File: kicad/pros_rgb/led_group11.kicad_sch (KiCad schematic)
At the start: 7 parts

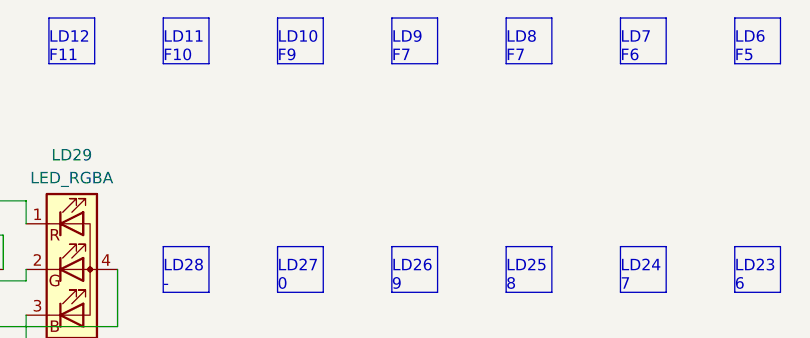
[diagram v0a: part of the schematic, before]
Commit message: kicad/pros_rgb: fix typos
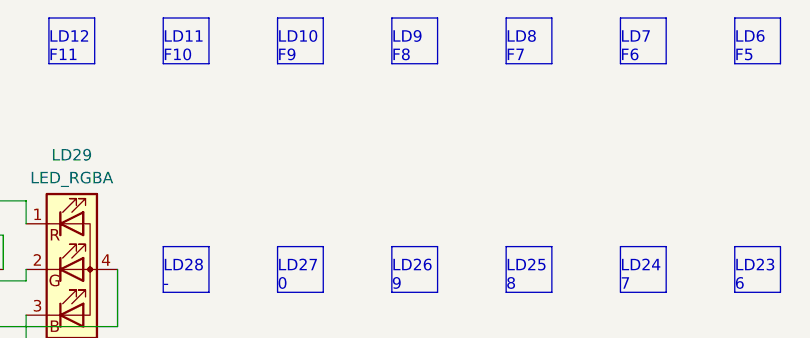
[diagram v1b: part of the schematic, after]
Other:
- note added: "LD9 F8"
- note removed: "LD9 F7"
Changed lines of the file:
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@@
     (effects (font (size 1.27 1.27)) (justify left bottom))
   )
-  (text "LD9\nF7" (at 157.48 29.21 0)
+  (text "LD9\nF8" (at 157.48 29.21 0)
     (effects (font (size 1.27 1.27)) (justify left bottom))
   )
